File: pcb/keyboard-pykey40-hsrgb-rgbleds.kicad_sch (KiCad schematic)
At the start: 107 parts, among them Q1 Q_NMOS_GSD

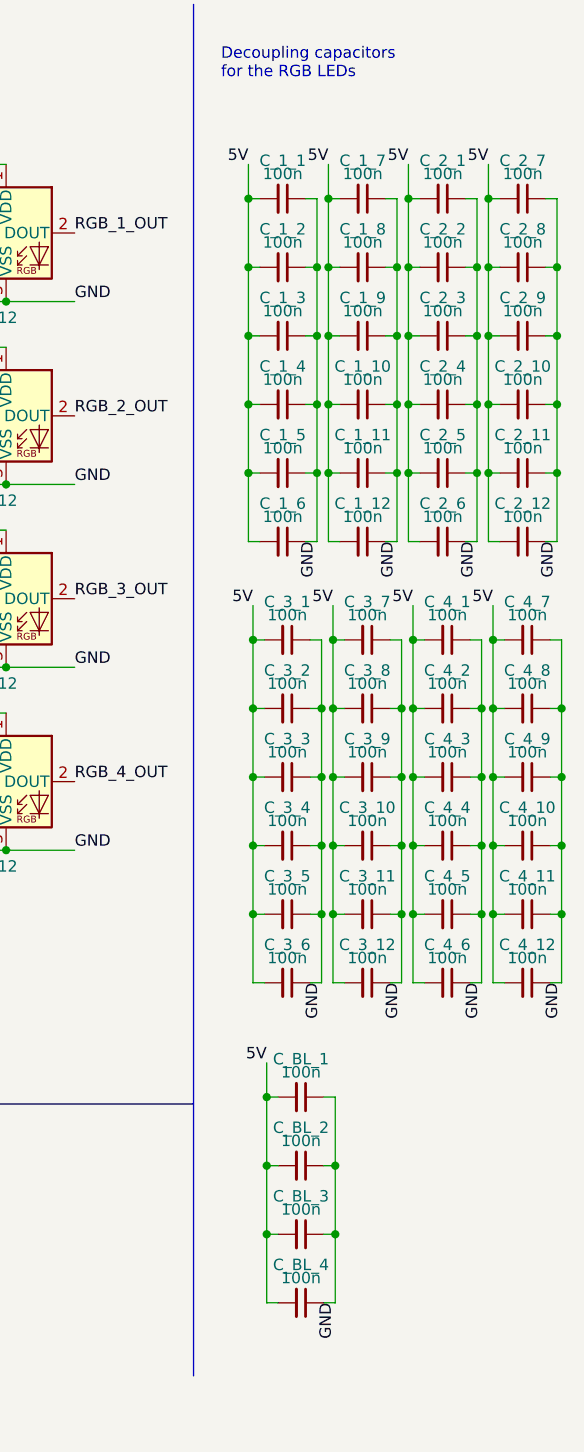
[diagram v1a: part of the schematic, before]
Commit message: pcb: tidy values in pykey40-hsrgb
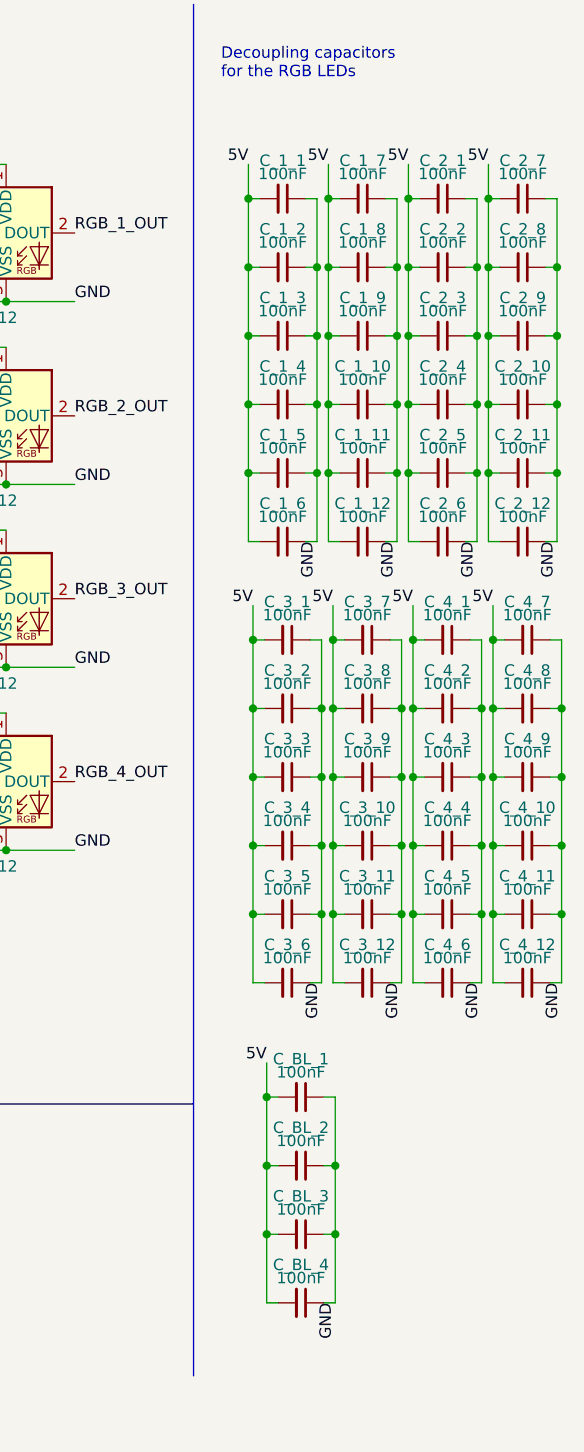
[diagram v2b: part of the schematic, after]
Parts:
- C_1_1, C_1_10, C_1_11, C_1_12, C_1_2, C_1_3, C_1_4, C_1_5, C_1_6, C_1_7, C_1_8, C_1_9, C_2_1, C_2_10, C_2_11, C_2_12, C_2_2, C_2_3, C_2_4, C_2_5, C_2_6, C_2_7, C_2_8, C_2_9, C_3_1, C_3_10, C_3_11, C_3_12, C_3_2, C_3_3, C_3_4, C_3_5, C_3_6, C_3_7, C_3_8, C_3_9, C_4_1, C_4_10, C_4_11, C_4_12, C_4_2, C_4_3, C_4_4, C_4_5, C_4_6, C_4_7, C_4_8, C_4_9, C_BL_1, C_BL_2, C_BL_3, C_BL_4: value 100n -> 100nF
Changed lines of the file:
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@@
 			)
 		)
-		(property "Value" "100n"
+		(property "Value" "100nF"
 			(at 262.89 79.8068 90)
 			(show_name no)
@@
 			)
 		)
-		(property "Value" "100n"
+		(property "Value" "100nF"
 			(at 262.89 110.2868 90)
 			(show_name no)
@@
 			)
 		)
-		(property "Value" "100n"
+		(property "Value" "100nF"
 			(at 244.602 38.4048 90)
 			(show_name no)
@@
 			)
 		)
-		(property "Value" "100n"
+		(property "Value" "100nF"
 			(at 235.712 68.8848 90)
 			(show_name no)
@@
 			)
 		)
-		(property "Value" "100n"
+		(property "Value" "100nF"
 			(at 253.492 38.4048 90)
 			(show_name no)
@@
 			)
 		)
-		(property "Value" "100n"
+		(property "Value" "100nF"
 			(at 236.22 110.2868 90)
 			(show_name no)
@@
 			)
 		)
-		(property "Value" "100n"
+		(property "Value" "100nF"
 			(at 262.382 30.7848 90)
 			(show_name no)
@@
 			)
 		)
-		(property "Value" "100n"
+		(property "Value" "100nF"
 			(at 237.744 145.8468 90)
 			(show_name no)
@@
 			)
 		)
-		(property "Value" "100n"
+		(property "Value" "100nF"
 			(at 235.712 30.7848 90)
 			(show_name no)
@@
 			)
 		)
-		(property "Value" "100n"
+		(property "Value" "100nF"
 			(at 236.22 79.8068 90)
 			(show_name no)
@@
 			)
 		)
-		(property "Value" "100n"
+		(property "Value" "100nF"
 			(at 262.89 95.0468 90)
 			(show_name no)
@@
 			)
 		)
-		(property "Value" "100n"
+		(property "Value" "100nF"
 			(at 253.492 68.8848 90)
 			(show_name no)
@@
 			)
 		)
-		(property "Value" "100n"
+		(property "Value" "100nF"
 			(at 237.744 138.2268 90)
 			(show_name no)
@@
 			)
 		)
-		(property "Value" "100n"
+		(property "Value" "100nF"
 			(at 235.712 61.2648 90)
 			(show_name no)
@@
 			)
 		)
-		(property "Value" "100n"
+		(property "Value" "100nF"
 			(at 262.382 68.8848 90)
 			(show_name no)
@@
 			)
 		)
-		(property "Value" "100n"
+		(property "Value" "100nF"
 			(at 236.22 102.6668 90)
 			(show_name no)
@@
 			)
 		)
-		(property "Value" "100n"
+		(property "Value" "100nF"
 			(at 262.89 102.6668 90)
 			(show_name no)
@@
 			)
 		)
-		(property "Value" "100n"
+		(property "Value" "100nF"
 			(at 254 110.2868 90)
 			(show_name no)
@@
 			)
 		)
-		(property "Value" "100n"
+		(property "Value" "100nF"
 			(at 236.22 87.4268 90)
 			(show_name no)
@@
 			)
 		)
-		(property "Value" "100n"
+		(property "Value" "100nF"
 			(at 244.602 61.2648 90)
 			(show_name no)
@@
 			)
 		)
-		(property "Value" "100n"
+		(property "Value" "100nF"
 			(at 235.712 46.0248 90)
 			(show_name no)
@@
 			)
 		)
-		(property "Value" "100n"
+		(property "Value" "100nF"
 			(at 244.602 68.8848 90)
 			(show_name no)
@@
 			)
 		)
-		(property "Value" "100n"
+		(property "Value" "100nF"
 			(at 254 95.0468 90)
 			(show_name no)
@@
 			)
 		)
-		(property "Value" "100n"
+		(property "Value" "100nF"
 			(at 262.89 117.9068 90)
 			(show_name no)
@@
 			)
 		)
-		(property "Value" "100n"
+		(property "Value" "100nF"
 			(at 244.602 30.7848 90)
 			(show_name no)
@@
 			)
 		)
-		(property "Value" "100n"
+		(property "Value" "100nF"
 			(at 245.11 110.2868 90)
 			(show_name no)
@@
 			)
 		)
-		(property "Value" "100n"
+		(property "Value" "100nF"
 			(at 262.382 61.2648 90)
 			(show_name no)
@@
 			)
 		)
-		(property "Value" "100n"
+		(property "Value" "100nF"
 			(at 262.382 38.4048 90)
 			(show_name no)
@@
 			)
 		)
-		(property "Value" "100n"
+		(property "Value" "100nF"
 			(at 262.89 87.4268 90)
 			(show_name no)
@@
 			)
 		)
-		(property "Value" "100n"
+		(property "Value" "100nF"
 			(at 254 102.6668 90)
 			(show_name no)
@@
 			)
 		)
-		(property "Value" "100n"
+		(property "Value" "100nF"
 			(at 245.11 95.0468 90)
 			(show_name no)
@@
 			)
 		)
-		(property "Value" "100n"
+		(property "Value" "100nF"
 			(at 245.11 87.4268 90)
 			(show_name no)
@@
 			)
 		)
-		(property "Value" "100n"
+		(property "Value" "100nF"
 			(at 236.22 117.9068 90)
 			(show_name no)
@@
 			)
 		)
-		(property "Value" "100n"
+		(property "Value" "100nF"
 			(at 245.11 102.6668 90)
 			(show_name no)
@@
 			)
 		)
-		(property "Value" "100n"
+		(property "Value" "100nF"
 			(at 253.492 30.7848 90)
 			(show_name no)
@@
 			)
 		)
-		(property "Value" "100n"
+		(property "Value" "100nF"
 			(at 235.712 38.4048 90)
 			(show_name no)
@@
 			)
 		)
-		(property "Value" "100n"
+		(property "Value" "100nF"
 			(at 262.382 53.6448 90)
 			(show_name no)
@@
 			)
 		)
-		(property "Value" "100n"
+		(property "Value" "100nF"
 			(at 253.492 53.6448 90)
 			(show_name no)
@@
 			)
 		)
-		(property "Value" "100n"
+		(property "Value" "100nF"
 			(at 244.602 53.6448 90)
 			(show_name no)
@@
 			)
 		)
-		(property "Value" "100n"
+		(property "Value" "100nF"
 			(at 236.22 95.0468 90)
 			(show_name no)
@@
 			)
 		)
-		(property "Value" "100n"
+		(property "Value" "100nF"
 			(at 254 79.8068 90)
 			(show_name no)
@@
 			)
 		)
-		(property "Value" "100n"
+		(property "Value" "100nF"
 			(at 254 87.4268 90)
 			(show_name no)
@@
 			)
 		)
-		(property "Value" "100n"
+		(property "Value" "100nF"
 			(at 262.382 46.0248 90)
 			(show_name no)
@@
 			)
 		)
-		(property "Value" "100n"
+		(property "Value" "100nF"
 			(at 237.744 153.4668 90)
 			(show_name no)
@@
 			)
 		)
-		(property "Value" "100n"
+		(property "Value" "100nF"
 			(at 253.492 46.0248 90)
 			(show_name no)
@@
 			)
 		)
-		(property "Value" "100n"
+		(property "Value" "100nF"
 			(at 253.492 61.2648 90)
 			(show_name no)
@@
 			)
 		)
-		(property "Value" "100n"
+		(property "Value" "100nF"
 			(at 245.11 79.8068 90)
 			(show_name no)
@@
 			)
 		)
-		(property "Value" "100n"
+		(property "Value" "100nF"
 			(at 244.602 46.0248 90)
 			(show_name no)
@@
 			)
 		)
-		(property "Value" "100n"
+		(property "Value" "100nF"
 			(at 237.744 130.6068 90)
 			(show_name no)
@@
 			)
 		)
-		(property "Value" "100n"
+		(property "Value" "100nF"
 			(at 235.712 53.6448 90)
 			(show_name no)
@@
 			)
 		)
-		(property "Value" "100n"
+		(property "Value" "100nF"
 			(at 254 117.9068 90)
 			(show_name no)
@@
 			)
 		)
-		(property "Value" "100n"
+		(property "Value" "100nF"
 			(at 245.11 117.9068 90)
 			(show_name no)
